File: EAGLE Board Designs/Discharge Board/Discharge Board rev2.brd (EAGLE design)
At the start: 60 x 76.7 mm, 27 parts, among them J100 CONNECTOR-5_MICRO_VS_, J101 CONNECTOR-2_MICROFIT_SMD_RIGH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, K1 RELAY_SPST_NC_POLARIZED_D_24

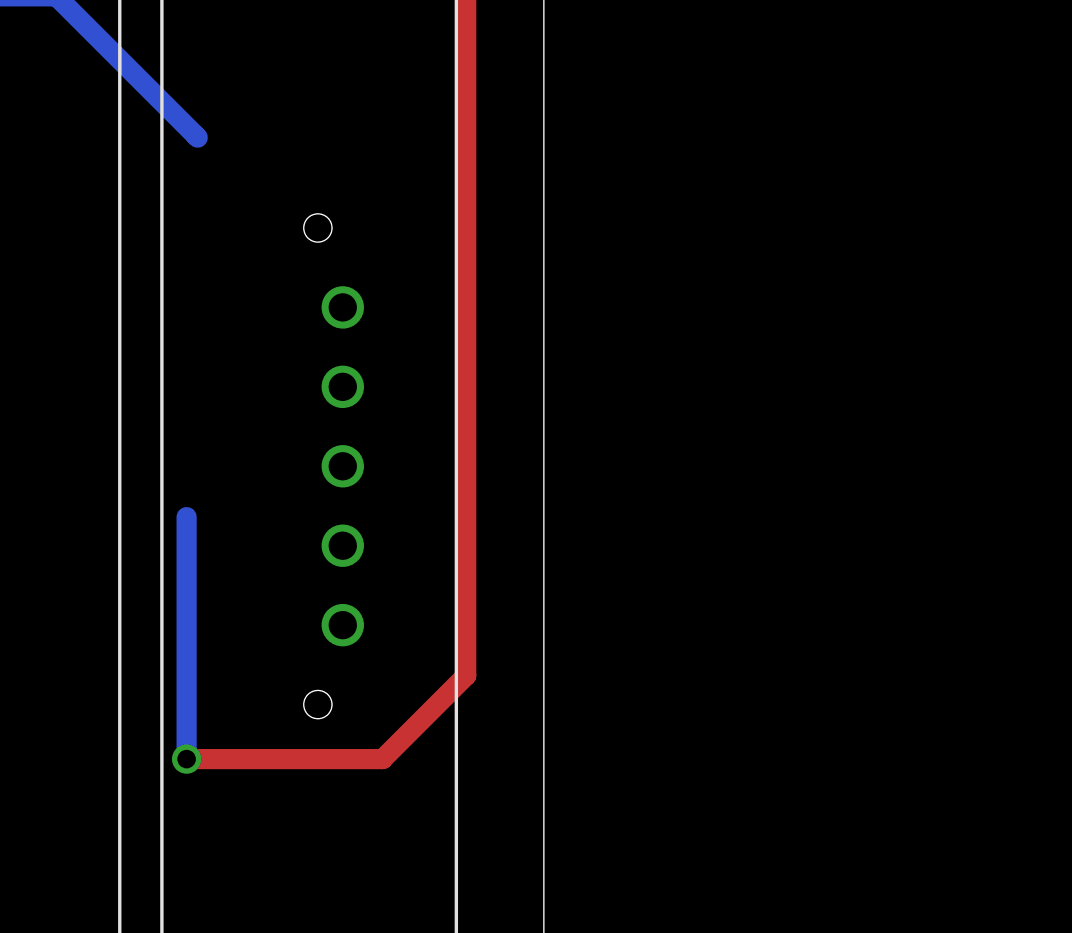
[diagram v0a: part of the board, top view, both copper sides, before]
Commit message: replaced 5-pin connector with new right angle
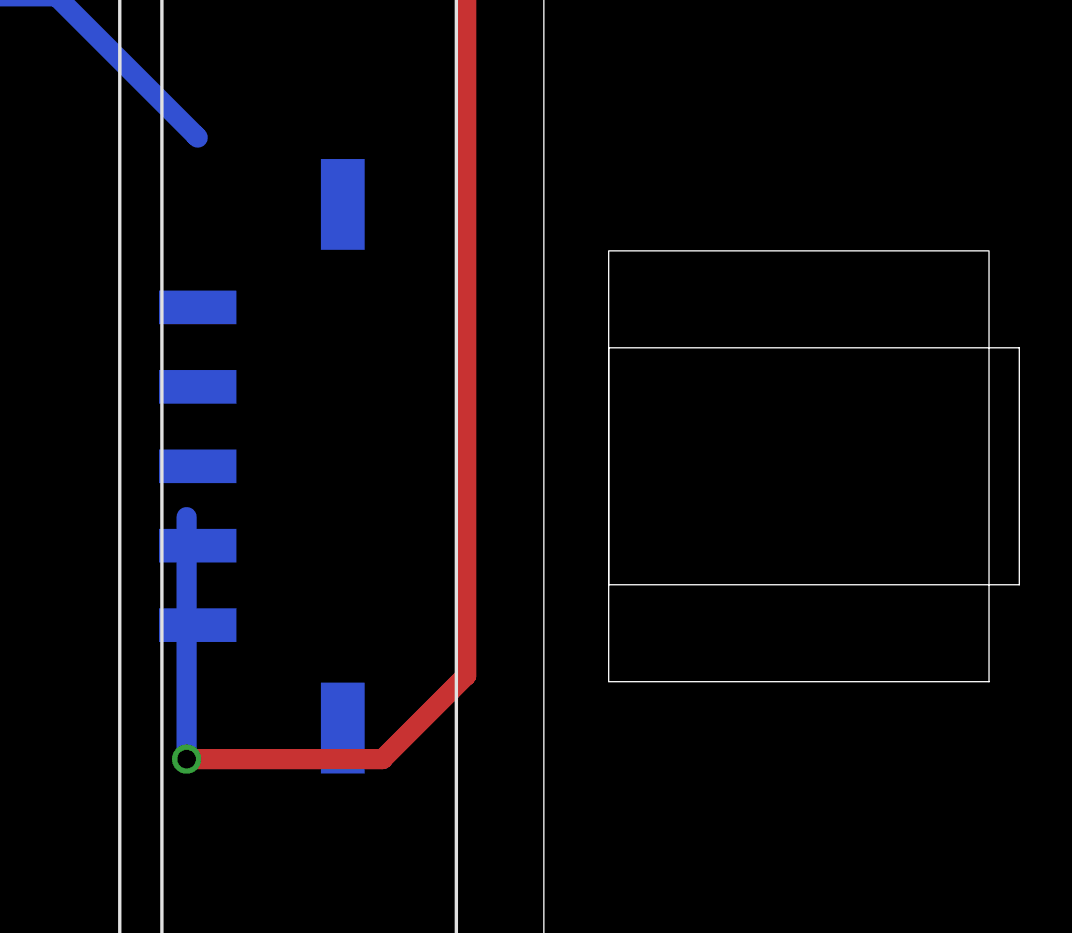
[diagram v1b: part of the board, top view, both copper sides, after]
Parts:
- J100: value CONNECTOR-5_MICRO_VS_ -> CONNECTOR-5_MICRO_R5S_; device HyTechDevices:MOLEX_MICROFIT_PTH_VERTICAL_05_SINGLE -> HyTechDevices:MOLEX_MICROFIT_SMD_RIGHTANGLE_05_SINGLE
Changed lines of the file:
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@@
 <attribute name="NAME" x="8.2296" y="29.5354" size="0.8128" layer="26" rot="MR0" align="bottom-center"/>
 </element>
-<element name="J100" library="HyTechDevices" package="MOLEX_MICROFIT_PTH_VERTICAL_05_SINGLE" value="CONNECTOR-5_MICRO_VS_" x="52.413" y="38.9644" smashed="yes" rot="MR270">
+<element name="J100" library="HyTechDevices" package="MOLEX_MICROFIT_SMD_RIGHTANGLE_05_SINGLE" value="CONNECTOR-5_MICRO_R5S_" x="52.413" y="38.9644" smashed="yes" rot="MR270">
 <attribute name="NAME" x="43.396" y="38.9898" size="0.8128" layer="26" rot="MR90" align="bottom-center"/>
 </element>
@@
 <contactref element="J100" pad="5"/>
 <contactref element="R4" pad="2"/>
-<wire x1="52.413" y1="32.97" x2="46.9393" y2="51.3667" width="0" layer="19" extent="16-16"/>
-<wire x1="-16.256" y1="-9.144" x2="52.413" y2="32.97" width="0" layer="19" extent="1-1"/>
+<wire x1="46.9393" y1="51.3667" x2="46.9393" y2="44.9588" width="0" layer="19" extent="16-16"/>
+<wire x1="-16.256" y1="-9.144" x2="46.9393" y2="44.9588" width="0" layer="19" extent="16-16"/>
 </signal>
 <signal name="N$51">
@@
 <contactref element="R5" pad="1"/>
 <contactref element="J100" pad="1"/>
-<wire x1="46.5202" y1="37.0467" x2="52.413" y2="44.9588" width="0" layer="19" extent="16-16"/>
+<wire x1="46.5202" y1="37.0467" x2="46.9393" y2="32.97" width="0" layer="19" extent="16-16"/>
 <wire x1="34.544" y1="-24.384" x2="46.5202" y2="27.9154" width="0" layer="19" extent="1-1"/>
 </signal>
@@
 <contactref element="J100" pad="2"/>
 <contactref element="R5" pad="2"/>
-<wire x1="-16.256" y1="-24.384" x2="52.413" y2="41.9616" width="0" layer="19" extent="1-1"/>
+<wire x1="-16.256" y1="-24.384" x2="46.9393" y2="35.9672" width="0" layer="19" extent="16-16"/>
 </signal>
 <signal name="N$2">
 <contactref element="J100" pad="4"/>
 <contactref element="R4" pad="1"/>
-<wire x1="34.544" y1="-9.144" x2="52.413" y2="35.9672" width="0" layer="19" extent="1-1"/>
+<wire x1="34.544" y1="-9.144" x2="46.9393" y2="41.9616" width="0" layer="19" extent="16-16"/>
 </signal>
 </signals>

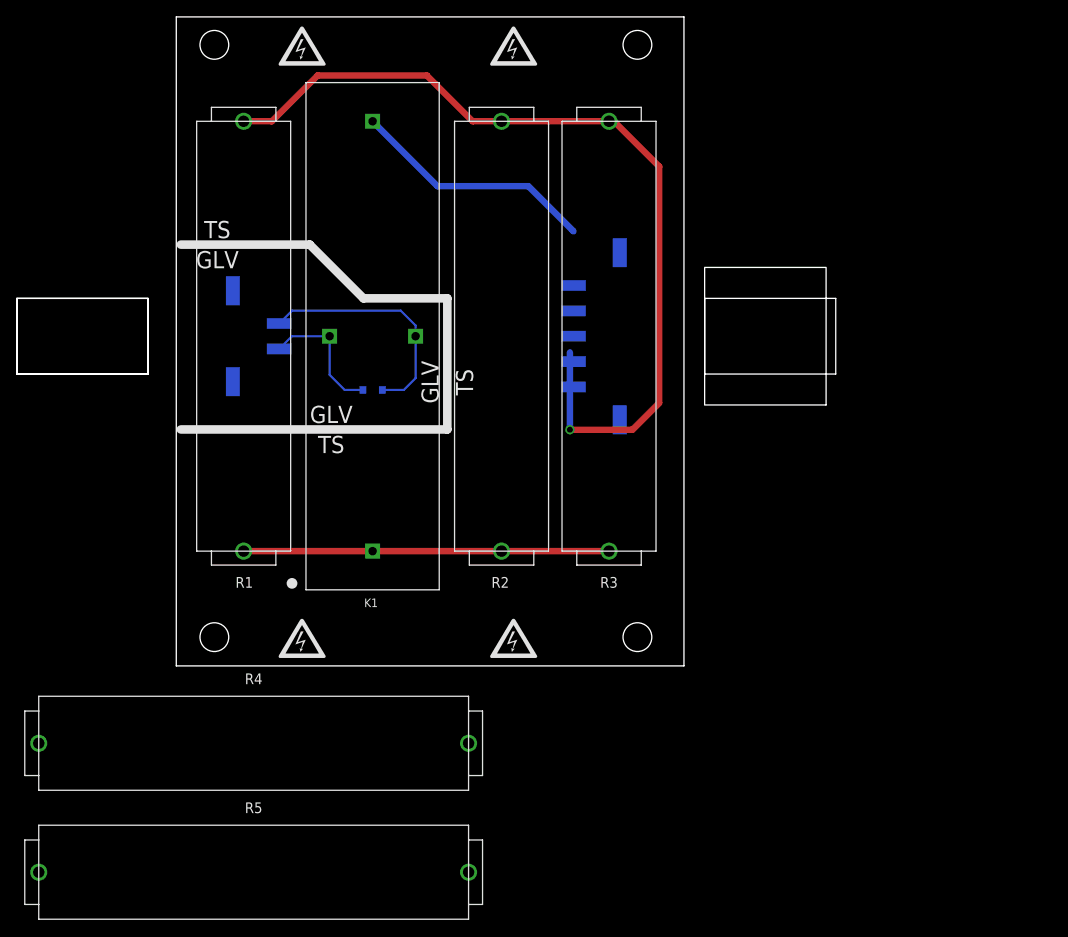
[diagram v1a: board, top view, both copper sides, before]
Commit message: move resistors
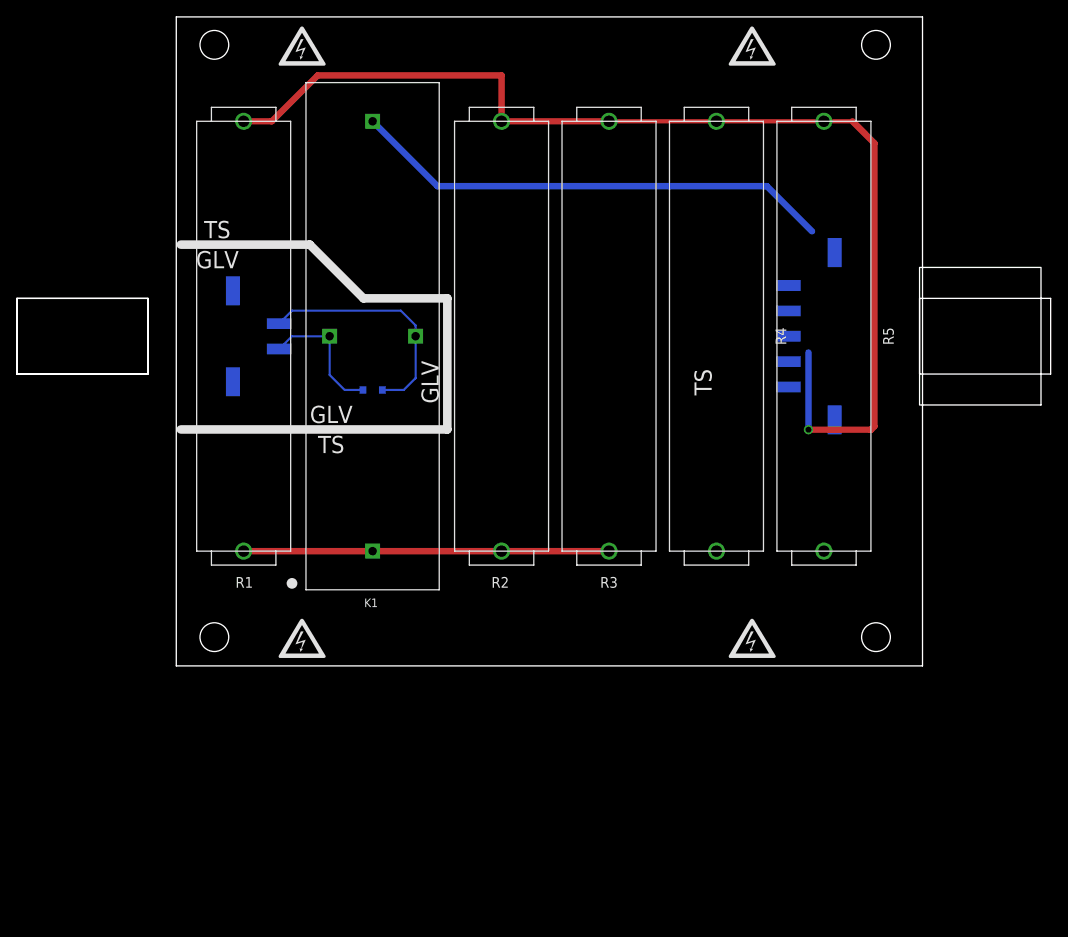
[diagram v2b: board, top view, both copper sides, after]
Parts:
- moved R5 92.5 mm to (76.5, 39.0), turned to 270 degrees
- moved R4 72.8 mm to (63.8, 39.0), turned to 270 degrees
- moved U$16 28.2 mm to (82.7, 3.40)
- moved U$18 28.2 mm to (82.7, 73.4)
- moved U$6 28.2 mm to (62.3, 33.5)
- moved U$10 28.2 mm to (68.1, 73.3)
- moved U$11 28.2 mm to (68.1, 73.3)
- moved U$13 28.2 mm to (68.1, 3.25)
- moved U$9 28.2 mm to (68.1, 3.25)
- moved J100 25.4 mm to (77.8, 39.0)
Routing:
- net TS-UNFUSED: track 104.8 -> 133.8 mm
- net TS+UNFUSED: track 29.1 -> 57.3 mm
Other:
- board size 60 x 76.7 mm -> 88.2 x 76.7 mm

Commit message: moved around resistors, think I found a decent wiring design
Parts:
- moved R5 0.11 mm to (76.6, 39.1)
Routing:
- net N$2: track 0.00 -> 36.8 mm
- net N$1: track 0.00 -> 34.7 mm, vias 0 -> 1
- net TS+UNFUSED: track 57.3 -> 65.2 mm
- net TS-UNFUSED: track 133.8 -> 131.0 mm, vias 1 -> 3
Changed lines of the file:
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@@
 <attribute name="VOLTAGE_MAX" value="750V" x="63.843" y="38.9644" size="1.778" layer="27" rot="R270" display="off"/>
 </element>
-<element name="R5" library="HyTechDevices" package="B20-SHORTENED" value="RESISTOR_B20-SHORTENED_15K" x="76.543" y="38.9644" smashed="yes" rot="R270">
-<attribute name="DKPN" value="B20J15KE-ND" x="76.543" y="38.9644" size="1.778" layer="27" rot="R270" display="off"/>
-<attribute name="MANUFACTURER" value="Ohmite" x="76.543" y="38.9644" size="1.778" layer="27" rot="R270" display="off"/>
-<attribute name="MOPN" value="588-B20J15KE" x="76.543" y="38.9644" size="1.778" layer="27" rot="R270" display="off"/>
-<attribute name="MPN" value="B20J15KE" x="76.543" y="38.9644" size="1.778" layer="27" rot="R270" display="off"/>
-<attribute name="NAME" x="83.528" y="38.9644" size="1.27" layer="21" font="vector" rot="R270" align="bottom-center"/>
-<attribute name="POWER" value="20W" x="76.543" y="38.9644" size="1.778" layer="27" rot="R270" display="off"/>
-<attribute name="RESISTANCE" value="15K" x="76.543" y="38.9644" size="1.778" layer="27" rot="R270" display="off"/>
-<attribute name="TOLERANCE" value="5%" x="76.543" y="38.9644" size="1.778" layer="27" rot="R270" display="off"/>
-<attribute name="VOLTAGE_CONTINUOUS" value="548V" x="76.543" y="38.9644" size="1.778" layer="27" rot="R270" display="off"/>
-<attribute name="VOLTAGE_MAX" value="750V" x="76.543" y="38.9644" size="1.778" layer="27" rot="R270" display="off"/>
+<element name="R5" library="HyTechDevices" package="B20-SHORTENED" value="RESISTOR_B20-SHORTENED_15K" x="76.5936" y="39.0644" smashed="yes" rot="R270">
+<attribute name="DKPN" value="B20J15KE-ND" x="76.5936" y="39.0644" size="1.778" layer="27" rot="R270" display="off"/>
+<attribute name="MANUFACTURER" value="Ohmite" x="76.5936" y="39.0644" size="1.778" layer="27" rot="R270" display="off"/>
+<attribute name="MOPN" value="588-B20J15KE" x="76.5936" y="39.0644" size="1.778" layer="27" rot="R270" display="off"/>
+<attribute name="MPN" value="B20J15KE" x="76.5936" y="39.0644" size="1.778" layer="27" rot="R270" display="off"/>
+<attribute name="NAME" x="83.5786" y="39.0644" size="1.27" layer="21" font="vector" rot="R270" align="bottom-center"/>
+<attribute name="POWER" value="20W" x="76.5936" y="39.0644" size="1.778" layer="27" rot="R270" display="off"/>
+<attribute name="RESISTANCE" value="15K" x="76.5936" y="39.0644" size="1.778" layer="27" rot="R270" display="off"/>
+<attribute name="TOLERANCE" value="5%" x="76.5936" y="39.0644" size="1.778" layer="27" rot="R270" display="off"/>
+<attribute name="VOLTAGE_CONTINUOUS" value="548V" x="76.5936" y="39.0644" size="1.778" layer="27" rot="R270" display="off"/>
+<attribute name="VOLTAGE_MAX" value="750V" x="76.5936" y="39.0644" size="1.778" layer="27" rot="R270" display="off"/>
 </element>
 </elements>
@@
 <signal name="TS+UNFUSED">
 <contactref element="K1" pad="2"/>
-<wire x1="23.203" y1="64.3644" x2="30.8702" y2="56.6972" width="0.762" layer="16"/>
-<wire x1="30.8702" y1="56.6972" x2="69.8028" y2="56.6972" width="0.762" layer="16"/>
-<wire x1="69.8028" y1="56.6972" x2="75.1333" y2="51.3667" width="0.762" layer="16"/>
 <contactref element="J100" pad="5"/>
 <contactref element="R4" pad="2"/>
-<wire x1="75.1333" y1="51.3667" x2="63.843" y2="64.3644" width="0" layer="19" extent="16-16"/>
-<wire x1="72.3393" y1="44.9588" x2="75.1333" y2="51.3667" width="0" layer="19" extent="16-16"/>
+<wire x1="23.203" y1="64.3644" x2="25.3866" y2="66.548" width="0.762" layer="16"/>
+<wire x1="63.843" y1="64.3644" x2="61.176671875" y2="66.548128125" width="0.762" layer="16"/>
+<wire x1="61.176671875" y1="66.548128125" x2="25.3866" y2="66.548" width="0.762" layer="16"/>
+<wire x1="72.2884" y1="45.0097" x2="72.3393" y2="44.9588" width="0.762" layer="16"/>
+<wire x1="63.843" y1="64.3644" x2="72.2884" y2="55.919" width="0.762" layer="16"/>
+<wire x1="72.2884" y1="55.919" x2="72.2884" y2="45.0097" width="0.762" layer="16"/>
 </signal>
 <signal name="N$51">
@@
 <wire x1="23.203" y1="13.5644" x2="38.443" y2="13.5644" width="0.762" layer="1"/>
 <wire x1="38.443" y1="13.5644" x2="51.143" y2="13.5644" width="0.762" layer="1"/>
-<wire x1="51.143" y1="13.5644" x2="23.203" y2="13.5644" width="0" layer="19"/>
 </signal>
 <signal name="TS-UNFUSED">
@@
 <contactref element="R2" pad="1"/>
 <contactref element="R3" pad="1"/>
-<wire x1="51.143" y1="64.3644" x2="38.443" y2="64.3644" width="0.762" layer="1"/>
 <wire x1="38.443" y1="64.3644" x2="38.443" y2="69.784" width="0.762" layer="1"/>
 <wire x1="38.443" y1="69.784" x2="16.71" y2="69.784" width="0.762" layer="1"/>
 <wire x1="16.71" y1="69.784" x2="11.2904" y2="64.3644" width="0.762" layer="1"/>
 <wire x1="11.2904" y1="64.3644" x2="7.963" y2="64.3644" width="0.762" layer="1"/>
-<wire x1="79.9212" y1="64.3644" x2="82.512" y2="61.7642" width="0.762" layer="1"/>
-<wire x1="51.143" y1="64.3644" x2="79.9212" y2="64.3644" width="0.508" layer="1"/>
-<wire x1="82.512" y1="61.7642" x2="82.512" y2="28.3254" width="0.762" layer="1"/>
-<wire x1="82.1114" y1="27.9154" x2="82.512" y2="28.3254" width="0.762" layer="1"/>
-<via x="74.7142" y="27.9154" extent="1-16" drill="0.7"/>
-<wire x1="74.7142" y1="27.9154" x2="82.1114" y2="27.9154" width="0.762" layer="1"/>
-<wire x1="74.7142" y1="27.9154" x2="74.7142" y2="37.0467" width="0.762" layer="16"/>
+<via x="76.67" y="21.7686" extent="1-16" drill="0.7"/>
 <contactref element="R5" pad="1"/>
 <contactref element="J100" pad="1"/>
-<wire x1="74.7142" y1="37.0467" x2="72.3393" y2="32.97" width="0" layer="19" extent="16-16"/>
-<wire x1="76.543" y1="13.5644" x2="74.7142" y2="27.9154" width="0" layer="19" extent="1-1"/>
+<wire x1="51.143" y1="64.3644" x2="51.7652" y2="64.3644" width="0.762" layer="1"/>
+<wire x1="38.443" y1="64.3644" x2="51.143" y2="64.3644" width="0.762" layer="1"/>
+<wire x1="76.5936" y1="21.6922" x2="76.67" y2="21.7686" width="0.762" layer="1"/>
+<wire x1="76.5936" y1="13.6644" x2="76.5936" y2="21.6922" width="0.762" layer="1"/>
+<wire x1="76.67" y1="21.7686" x2="76.67" y2="26.0984" width="0.762" layer="1"/>
+<wire x1="76.67" y1="26.0984" x2="76.6572" y2="26.1112" width="0.762" layer="1"/>
+<via x="76.6572" y="26.1112" extent="1-16" drill="0.3556"/>
+<wire x1="51.143" y1="64.3644" x2="51.2818" y2="64.3644" width="0.762" layer="1"/>
+<wire x1="61.3918" y1="54.2544" x2="51.2818" y2="64.3644" width="0.762" layer="1"/>
+<wire x1="69.3166" y1="26.4668" x2="61.5442" y2="26.4668" width="0.762" layer="1"/>
+<wire x1="61.5442" y1="26.4668" x2="61.3918" y2="26.6192" width="0.762" layer="1"/>
+<wire x1="61.3918" y1="54.2544" x2="61.3918" y2="26.6192" width="0.762" layer="1"/>
+<via x="69.3166" y="26.4668" extent="1-16" drill="0.3556"/>
+<wire x1="69.3166" y1="26.4668" x2="76.3016" y2="26.4668" width="0.762" layer="16"/>
+<wire x1="76.3016" y1="26.4668" x2="76.6572" y2="26.1112" width="0.762" layer="16"/>
+<wire x1="69.3166" y1="26.4668" x2="72.3393" y2="26.4668" width="0.762" layer="16"/>
+<wire x1="72.3393" y1="26.4668" x2="72.3393" y2="32.97" width="0.762" layer="16"/>
 </signal>
 <signal name="N$1">
 <contactref element="J100" pad="2"/>
 <contactref element="R5" pad="2"/>
-<wire x1="72.3393" y1="35.9672" x2="76.543" y2="64.3644" width="0" layer="19" extent="16-16"/>
+<wire x1="76.5936" y1="64.4644" x2="69.2658" y2="57.1366" width="0.762" layer="1"/>
+<wire x1="69.2658" y1="57.1366" x2="69.2658" y2="35.8902" width="0.762" layer="1"/>
+<via x="69.2658" y="35.8902" extent="1-16" drill="0.3556"/>
+<wire x1="69.2658" y1="35.8902" x2="69.3428" y2="35.9672" width="0.762" layer="16"/>
+<wire x1="69.3428" y1="35.9672" x2="72.3393" y2="35.9672" width="0.762" layer="16"/>
 </signal>
 <signal name="N$2">
 <contactref element="J100" pad="4"/>
 <contactref element="R4" pad="1"/>
-<wire x1="63.843" y1="13.5644" x2="72.3393" y2="41.9616" width="0" layer="19" extent="16-16"/>
+<wire x1="63.843" y1="13.5644" x2="63.843" y2="41.7704" width="0.762" layer="16"/>
+<wire x1="63.843" y1="41.7704" x2="64.0588" y2="41.9862" width="0.762" layer="16"/>
+<wire x1="64.0588" y1="41.9862" x2="72.3147" y2="41.9862" width="0.762" layer="16"/>
+<wire x1="72.3147" y1="41.9862" x2="72.3393" y2="41.9616" width="0.762" layer="16"/>
 </signal>
 </signals>
